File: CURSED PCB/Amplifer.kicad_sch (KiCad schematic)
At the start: 8 parts, among them U6 OPA196xDBV, U7 MCP3562-E_ST

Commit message: fixed issue with mcu
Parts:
- U6: value OPA196xDBV -> OPA323
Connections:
- net +3.3VA: now also U7.4 (REFIN+)
- net GND: no longer U7.4 (REFIN+)
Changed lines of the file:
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@@
 	)
 	(junction
-		(at 227.33 77.47)
+		(at 229.87 71.12)
 		(diameter 0)
 		(color 0 0 0 0)
 	)
 	(junction
-		(at 227.33 80.01)
+		(at 228.6 77.47)
 		(diameter 0)
 		(color 0 0 0 0)
@@
 	(wire
 		(pts
-			(xy 229.87 77.47) (xy 227.33 77.47)
-		)
-		(stroke
-			(width 0)
-			(type default)
-		)
-	)
-	(wire
-		(pts
 			(xy 260.35 85.09) (xy 265.43 85.09)
 		)
@@
 	(wire
 		(pts
+			(xy 227.33 71.12) (xy 229.87 71.12)
+		)
+		(stroke
+			(width 0)
+			(type default)
+		)
+	)
+	(wire
+		(pts
 			(xy 146.05 73.66) (xy 144.78 73.66)
 		)
@@
 	(wire
 		(pts
+			(xy 229.87 71.12) (xy 229.87 74.93)
+		)
+		(stroke
+			(width 0)
+			(type default)
+		)
+	)
+	(wire
+		(pts
 			(xy 260.35 80.01) (xy 265.43 80.01)
 		)
@@
 	(wire
 		(pts
-			(xy 227.33 82.55) (xy 227.33 80.01)
-		)
-		(stroke
-			(width 0)
-			(type default)
-		)
-	)
-	(wire
-		(pts
-			(xy 267.97 77.47) (xy 267.97 72.39)
+			(xy 228.6 77.47) (xy 229.87 77.47)
+		)
+		(stroke
+			(width 0)
+			(type default)
+		)
+	)
+	(wire
+		(pts
+			(xy 229.87 80.01) (xy 228.6 80.01)
+		)
+		(stroke
+			(width 0)
+			(type default)
+		)
+	)
+	(wire
+		(pts
+			(xy 279.4 77.47) (xy 279.4 78.74)
 		)
 		(stroke
@@
 	(wire
 		(pts
-			(xy 229.87 50.8) (xy 229.87 74.93)
+			(xy 227.33 71.12) (xy 227.33 82.55)
+		)
+		(stroke
+			(width 0)
+			(type default)
+		)
+	)
+	(wire
+		(pts
+			(xy 229.87 50.8) (xy 229.87 71.12)
 		)
 		(stroke
@@
 	(wire
 		(pts
-			(xy 227.33 80.01) (xy 227.33 77.47)
-		)
-		(stroke
-			(width 0)
-			(type default)
-		)
-	)
-	(wire
-		(pts
-			(xy 229.87 80.01) (xy 227.33 80.01)
-		)
-		(stroke
-			(width 0)
-			(type default)
-		)
-	)
-	(wire
-		(pts
 			(xy 153.67 60.96) (xy 153.67 73.66)
 		)
@@
 	(wire
 		(pts
-			(xy 260.35 77.47) (xy 267.97 77.47)
+			(xy 260.35 77.47) (xy 279.4 77.47)
 		)
 		(stroke
@@
 	(wire
 		(pts
-			(xy 227.33 77.47) (xy 222.25 77.47)
+			(xy 222.25 77.47) (xy 228.6 77.47)
+		)
+		(stroke
+			(width 0)
+			(type default)
+		)
+	)
+	(wire
+		(pts
+			(xy 228.6 80.01) (xy 228.6 77.47)
 		)
 		(stroke
@@
 			)
 		)
-		(property "Value" "OPA196xDBV"
+		(property "Value" "OPA323"
 			(at 150.5519 92.71 0)
 			(effects
@@
 	(symbol
 		(lib_id "power:GND")
-		(at 267.97 72.39 180)
+		(at 279.4 78.74 0)
 		(unit 1)
 		(exclude_from_sim no)
@@
 		(fields_autoplaced yes)
 		(property "Reference" "#PWR044"
-			(at 267.97 66.04 0)
+			(at 279.4 85.09 0)
 			(effects
 				(font
@@
 		)
 		(property "Value" "GND"
-			(at 267.97 67.31 0)
-			(effects
-				(font
-					(size 1.27 1.27)
-				)
+			(at 281.94 80.0099 0)
+			(effects
+				(font
+					(size 1.27 1.27)
+				)
+				(justify left)
 			)
 		)
 		(property "Footprint" ""
-			(at 267.97 72.39 0)
+			(at 279.4 78.74 0)
 			(effects
 				(font
@@
 		)
 		(property "Datasheet" ""
-			(at 267.97 72.39 0)
+			(at 279.4 78.74 0)
 			(effects
 				(font
@@
 		)
 		(property "Description" "Power symbol creates a global label with name \"GND\" , ground"
-			(at 267.97 72.39 0)
-			(effects
-				(font
+			(at 279.4 78.74 0)
+			(effects
+				(font

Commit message: something something fixes to something related
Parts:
- U7: footprint canhw_footprints:TSSOP20_ST_MCH -> (none)
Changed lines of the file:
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@@
 			)
 		)
-		(property "Footprint" "canhw_footprints:TSSOP20_ST_MCH"
+		(property "Footprint" ""
 			(at 245.11 86.36 0)
 			(effects

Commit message: fixed errors
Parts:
- U7: footprint (none) -> Package_SO:TSSOP-20_4.4x6.5mm_P0.65mm
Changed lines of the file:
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@@
 	(wire
 		(pts
-			(xy 260.35 92.71) (xy 265.43 92.71)
-		)
-		(stroke
-			(width 0)
-			(type default)
-		)
-	)
-	(wire
-		(pts
-			(xy 260.35 85.09) (xy 265.43 85.09)
+			(xy 260.35 92.71) (xy 267.97 92.71)
+		)
+		(stroke
+			(width 0)
+			(type default)
+		)
+	)
+	(wire
+		(pts
+			(xy 260.35 85.09) (xy 267.97 85.09)
 		)
 		(stroke
@@
 	(wire
 		(pts
-			(xy 260.35 82.55) (xy 265.43 82.55)
+			(xy 260.35 82.55) (xy 267.97 82.55)
 		)
 		(stroke
@@
 	(wire
 		(pts
-			(xy 260.35 80.01) (xy 265.43 80.01)
+			(xy 260.35 80.01) (xy 267.97 80.01)
 		)
 		(stroke
@@
 	(wire
 		(pts
-			(xy 260.35 90.17) (xy 265.43 90.17)
+			(xy 260.35 90.17) (xy 267.97 90.17)
 		)
 		(stroke
@@
 	(wire
 		(pts
-			(xy 260.35 87.63) (xy 265.43 87.63)
-		)
-		(stroke
-			(width 0)
-			(type default)
-		)
-	)
-	(hierarchical_label "MKLKIN"
+			(xy 260.35 87.63) (xy 267.97 87.63)
+		)
+		(stroke
+			(width 0)
+			(type default)
+		)
+	)
+	(hierarchical_label "SCLK"
 		(shape input)
-		(at 265.43 80.01 0)
+		(at 267.97 90.17 0)
 		(effects
 			(font
@@
 		)
 	)
-	(hierarchical_label "CS"
+	(hierarchical_label "SDO"
 		(shape input)
-		(at 265.43 92.71 0)
+		(at 267.97 85.09 0)
 		(effects
 			(font
@@
 		)
 	)
-	(hierarchical_label "SDO"
+	(hierarchical_label "SDI"
 		(shape input)
-		(at 265.43 85.09 0)
+		(at 267.97 87.63 0)
 		(effects
 			(font
@@
 		)
 	)
-	(hierarchical_label "SDI"
+	(hierarchical_label "MKLKIN"
 		(shape input)
-		(at 265.43 87.63 0)
+		(at 267.97 80.01 0)
 		(effects
 			(font
@@
 		)
 	)
-	(hierarchical_label "SCLK"
+	(hierarchical_label "IRQ{slash}MDAT"
 		(shape input)
-		(at 265.43 90.17 0)
+		(at 267.97 82.55 0)
 		(effects
 			(font
@@
 		)
 	)
-	(hierarchical_label "IRQ{slash}MDAT"
+	(hierarchical_label "CS"
 		(shape input)
-		(at 265.43 82.55 0)
+		(at 267.97 92.71 0)
 		(effects
 			(font
@@
 			)
 		)
-		(property "Footprint" ""
+		(property "Footprint" "Package_SO:TSSOP-20_4.4x6.5mm_P0.65mm"
 			(at 245.11 86.36 0)
 			(effects

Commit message: file
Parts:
- C14, C15: footprint Capacitor_SMD:C_0201_0603Metric_Pad0.64x0.40mm_HandSolder -> Capacitor_SMD:C_0603_1608Metric_Pad1.08x0.95mm_HandSolder
- R7, R8, R9: footprint Resistor_SMD:R_0201_0603Metric -> Resistor_SMD:R_0603_1608Metric_Pad0.98x0.95mm_HandSolder
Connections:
- net 5VA renamed 5V
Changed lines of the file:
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@@
 			)
 		)
-		(property "Footprint" "Capacitor_SMD:C_0201_0603Metric_Pad0.64x0.40mm_HandSolder"
+		(property "Footprint" "Capacitor_SMD:C_0603_1608Metric_Pad1.08x0.95mm_HandSolder"
 			(at 154.94 124.46 0)
 			(effects
@@
 			)
 		)
-		(property "Footprint" "Resistor_SMD:R_0201_0603Metric"
+		(property "Footprint" "Resistor_SMD:R_0603_1608Metric_Pad0.98x0.95mm_HandSolder"
 			(at 149.606 74.676 90)
 			(effects
@@
 			)
 		)
-		(property "Value" "5VA"
+		(property "Value" "5V"
 			(at 153.67 50.8 0)
 			(effects
@@
 			)
 		)
-		(property "Footprint" "Capacitor_SMD:C_0201_0603Metric_Pad0.64x0.40mm_HandSolder"
+		(property "Footprint" "Capacitor_SMD:C_0603_1608Metric_Pad1.08x0.95mm_HandSolder"
 			(at 135.89 66.04 0)
 			(effects
@@
 			)
 		)
-		(property "Footprint" "Resistor_SMD:R_0201_0603Metric"
+		(property "Footprint" "Resistor_SMD:R_0603_1608Metric_Pad0.98x0.95mm_HandSolder"
 			(at 145.796 66.294 90)
 			(effects
@@
 			)
 		)
-		(property "Footprint" "Resistor_SMD:R_0201_0603Metric"
+		(property "Footprint" "Resistor_SMD:R_0603_1608Metric_Pad0.98x0.95mm_HandSolder"
 			(at 155.194 108.966 90)
 			(effects

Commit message: connected stuff for pcb
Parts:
- D4: value BPW34 -> ODD-5WISOL
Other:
- note removed: "Amplifer Ref: https://www.ti.com/lit/an/sboa220b/sboa220b.pdf?ts=1747595142490 Photodode ref: https://www.ti.com/lit/ug/tiduaz1/tiduaz1.pdf Left to do: Add amount for capactiors and resistiors Maybe add anti-analising filter after the amplifier output?"
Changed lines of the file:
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@@
 	(generator_version "9.0")
 	(paper "A4")
-	(text "Amplifer Ref:\nhttps://www.ti.com/lit/an/sboa220b/sboa220b.pdf?ts=1747595142490\n\nPhotodode ref: \nhttps://www.ti.com/lit/ug/tiduaz1/tiduaz1.pdf\n\nLeft to do:\nAdd amount for capactiors and resistiors\n\nMaybe add anti-analising filter after the amplifier output?"
-		(exclude_from_sim no)
-		(at 13.716 115.062 0)
-		(effects
-			(font
-				(size 1.27 1.27)
-			)
-			(justify left)
-			(href "#3")
-		)
-	)
 	(junction
 		(at 134.62 107.95)
@@
 			)
 		)
-		(property "Value" "BPW34"
+		(property "Value" "ODD-5WISOL"
 			(at 96.52 93.0528 90)
 			(effects

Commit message: redone pcb
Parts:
- added C16, C22: 0.1uF, Capacitor_SMD:C_0805_2012Metric_Pad1.18x1.45mm_HandSolder, symbol Device:C_Small
- added C21, C23: 10uF, Capacitor_SMD:C_0805_2012Metric_Pad1.18x1.45mm_HandSolder, symbol Device:C_Small
- C14, C15: footprint Capacitor_SMD:C_0603_1608Metric_Pad1.08x0.95mm_HandSolder -> Capacitor_SMD:C_0805_2012Metric_Pad1.18x1.45mm_HandSolder
- D4: footprint OptoDevice:Osram_DIL2_4.3x4.65mm_P5.08mm -> Package_TO_SOT_THT:TO-5-3
- R7, R8, R9: footprint Resistor_SMD:R_0603_1608Metric_Pad0.98x0.95mm_HandSolder -> Resistor_SMD:R_0805_2012Metric_Pad1.20x1.40mm_HandSolder
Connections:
- net +3.3VA: now also C16.1, C21.1
- net +3.3VD: now also C22.1, C23.1
- net GND: now also C22.2, C23.2; no longer D4.2 (A), U6.2 (V-), U7.2 (AGND), U7.3 (REFIN-)
- net at C15.1, D4.1 (K), R9.1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: now also D4.3 (Cathode_2)
- net 5V renamed +5V
- new net AGND: C16.2, C21.2, D4.2 (A), U6.2 (V-), U7.2 (AGND), U7.3 (REFIN-)

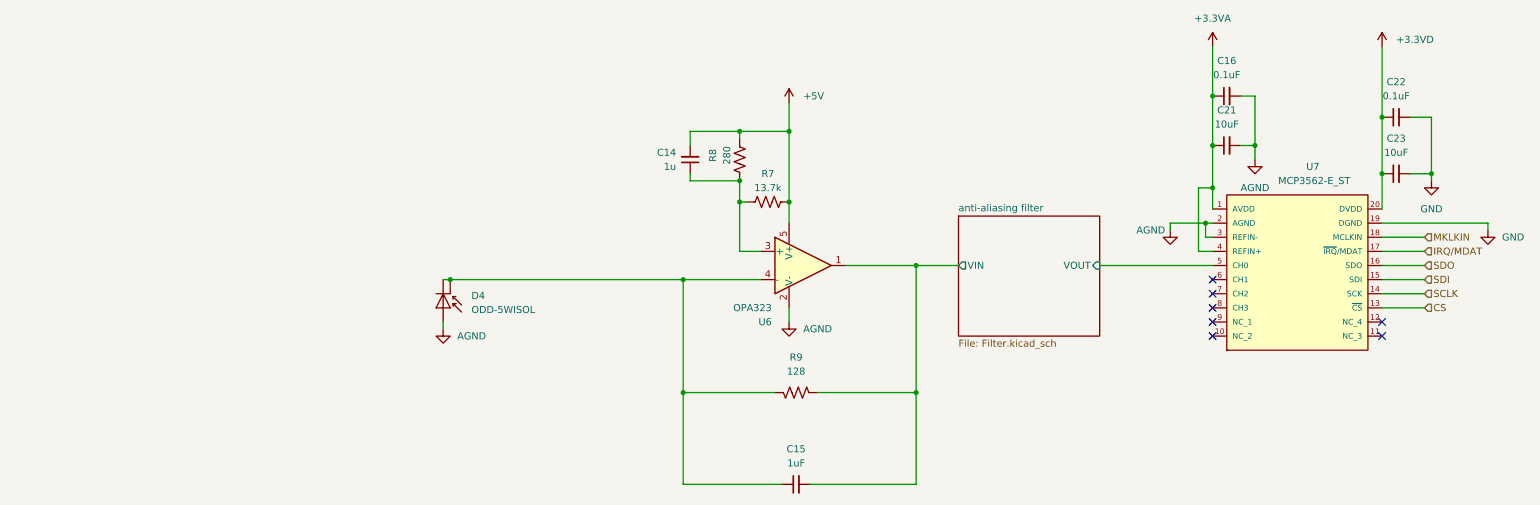
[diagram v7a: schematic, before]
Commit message: no spilt-ground plane (bad idea)
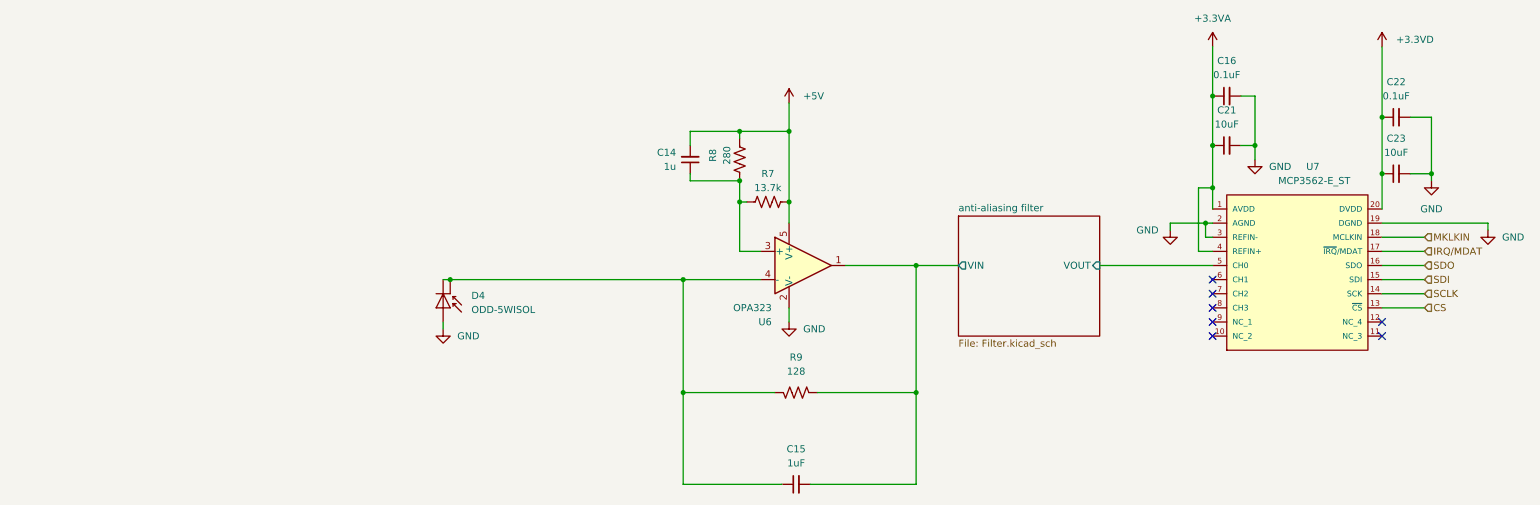
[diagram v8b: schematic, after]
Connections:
- net AGND is gone; now on net GND: C16.2, C21.2, D4.2 (A), U6.2 (V-), U7.2 (AGND), U7.3 (REFIN-)
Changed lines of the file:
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@@
 			)
 		)
-		(property "Value" "AGND"
-			(at 237.49 71.12 0)
-			(effects
-				(font
-					(size 1.27 1.27)
-				)
+		(property "Value" "GND"
+			(at 240.03 67.3099 0)
+			(effects
+				(font
+					(size 1.27 1.27)
+				)
+				(justify left)
 			)
 		)
@@
 			)
 		)
-		(property "Value" "AGND"
+		(property "Value" "GND"
 			(at 216.154 78.74 0)
 			(effects
@@
 			)
 		)
-		(property "Value" "AGND"
+		(property "Value" "GND"
 			(at 93.98 97.7899 0)
 			(effects
@@
 			)
 		)
-		(property "Value" "AGND"
+		(property "Value" "GND"
 			(at 156.21 96.5199 0)
 			(effects
